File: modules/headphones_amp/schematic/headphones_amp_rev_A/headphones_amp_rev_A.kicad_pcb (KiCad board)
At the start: 2 copper layers, 120 x 100 mm, 127 parts, among them J1 AudioJack3_SwitchTR, J2 AudioJack3_SwitchTR, J3 Conn_01x02, J4 Conn_01x02, J5 Conn_01x02, J6 Conn_01x02, J7 Conn_01x02, Q1 BC140, Q10 BC548, Q11 BC548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

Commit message: input stage: improved biasing (more stable version), added component values (validated on prototype) PCB cleanup (useless footprints)
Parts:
- removed C16, C18: 220µ, Capacitor_THT:CP_Radial_D10.0mm_P5.00mm
- removed the D1 at (269.6, 64.6)
- removed the D2 at (324.6, 161.2)
- removed D3: 1N4148, Diode_THT:D_DO-35_SOD27_P7.62mm_Horizontal
- removed the R18 at (110.2, 67.7)
- removed the R23 at (81.8, 108.2)
- removed the R24 at (31.0, 76.0)
- removed the R36 at (48.9, 34.9)
- removed the R4 at (237.8, 50.9)
- removed the R45 at (31.0, 80.0)
- removed R47, R49: 470, Resistor_THT:R_Axial_DIN0207_L6.3mm_D2.5mm_P10.16mm_Horizontal
- removed the SW1 at (141.0, 27.2)
- C10, C3, C9: value 220µ -> 33µF
- C15, C17: value 47µF -> 33µF
- R22, R50: value 470 -> 5.6k
- R23, R48: value 470 -> 4.7k
- R24, R4, R45, R46: value 470 -> 100k
- R36, R51: value 470 -> 2.7k
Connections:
- R24 pad 1: +12V -> Net-(Q18-C)
- R4 pad 1: +12V -> Net-(Q17-C)
- RV3 pad 4: GND -> Net-(J4-Pin_2)
- RV3 pad 6: Net-(J4-Pin_2) -> GND

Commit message: updated pcb layout
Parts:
- moved R3 243.8 mm to (14.4, 144.3)
- moved R5 243.8 mm to (14.4, 152.4)
- moved R8 243.8 mm to (14.4, 164.6)
- moved TP3 243.8 mm to (35.6, 124.5)
- moved R23 163.2 mm to (26.7, 79.0)
- moved R24 163.2 mm to (26.7, 83.0)
- moved R36 163.2 mm to (26.7, 87.1)
- moved R4 163.2 mm to (26.7, 74.9)
- moved R45 163.2 mm to (26.7, 91.1)
- moved R46 163.2 mm to (26.7, 95.2)
- moved R48 163.2 mm to (26.7, 103.3)
- moved R50 163.2 mm to (26.7, 111.4)
- moved R51 163.2 mm to (26.7, 115.4)
- moved C15 163.2 mm to (16.8, 78.7)
- moved C17 163.2 mm to (16.8, 101.8)
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
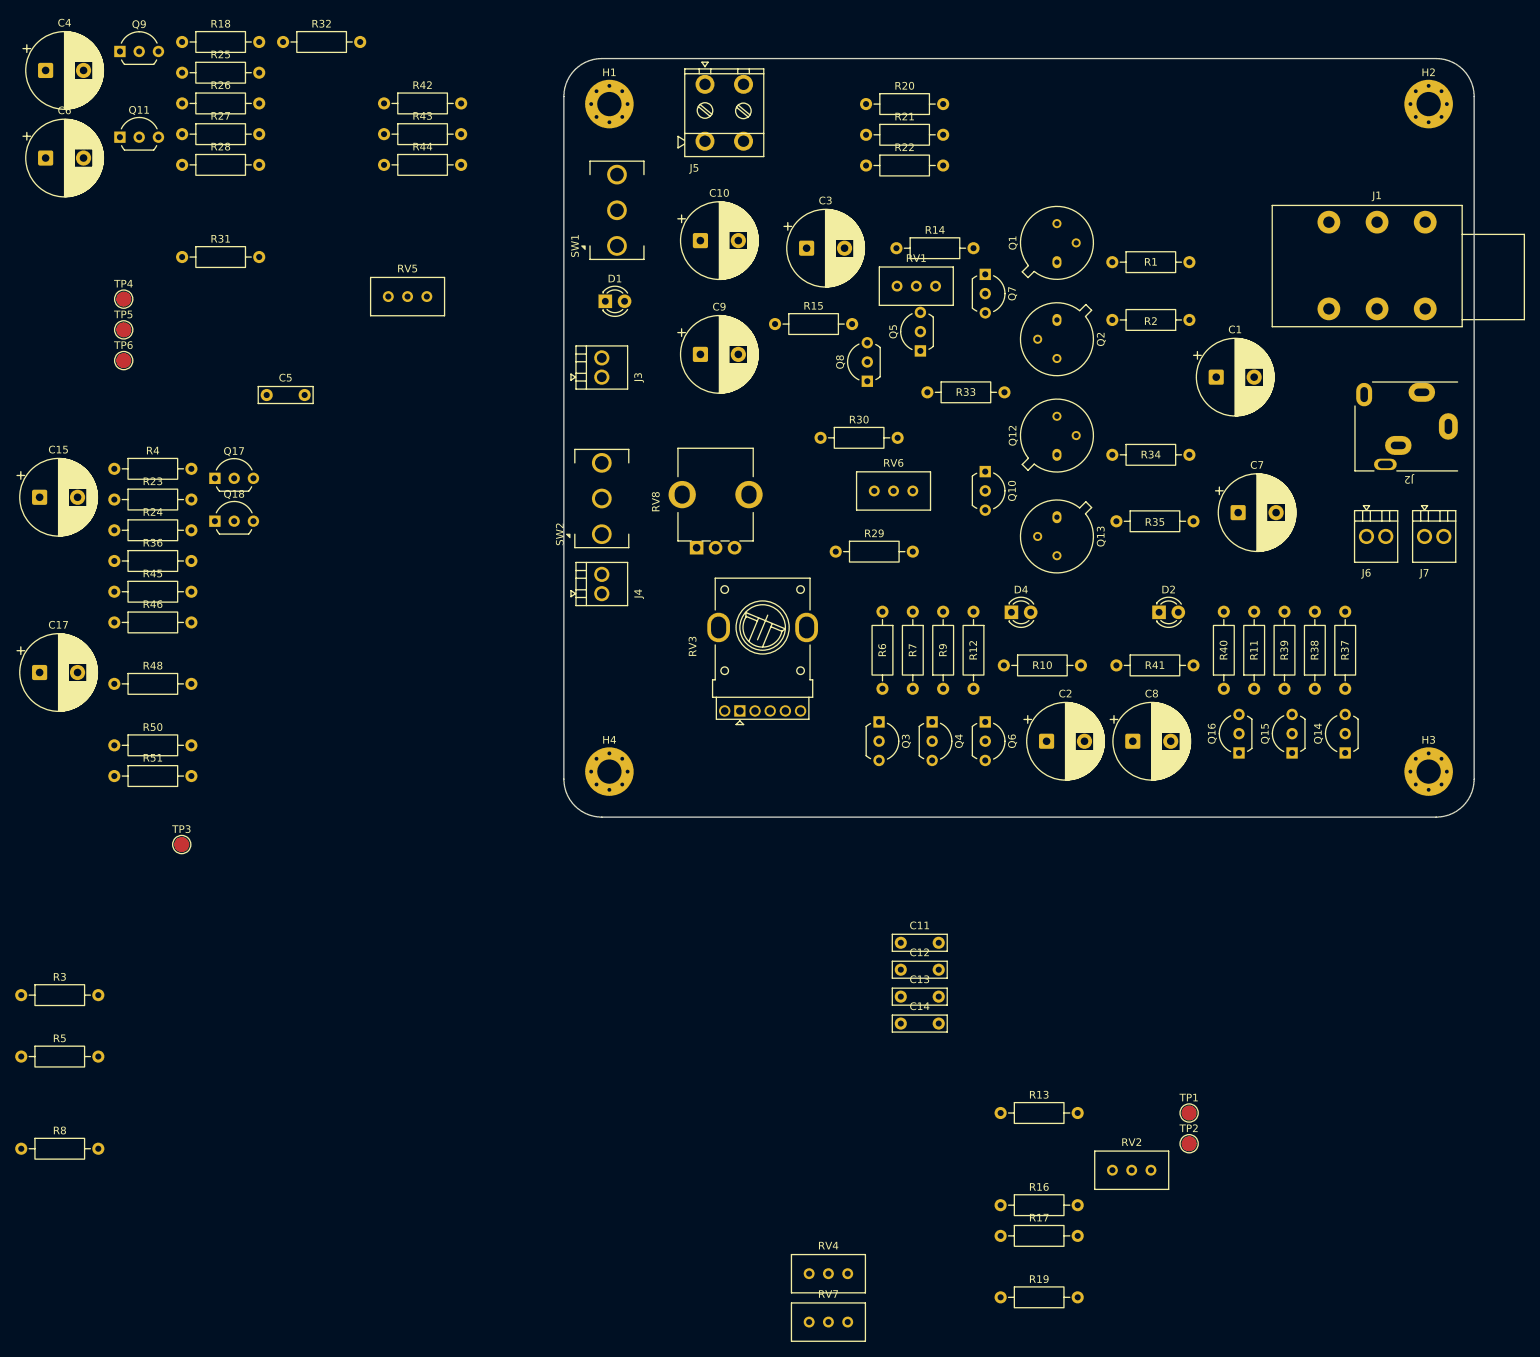
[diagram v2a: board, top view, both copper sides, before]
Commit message: added on board measurements
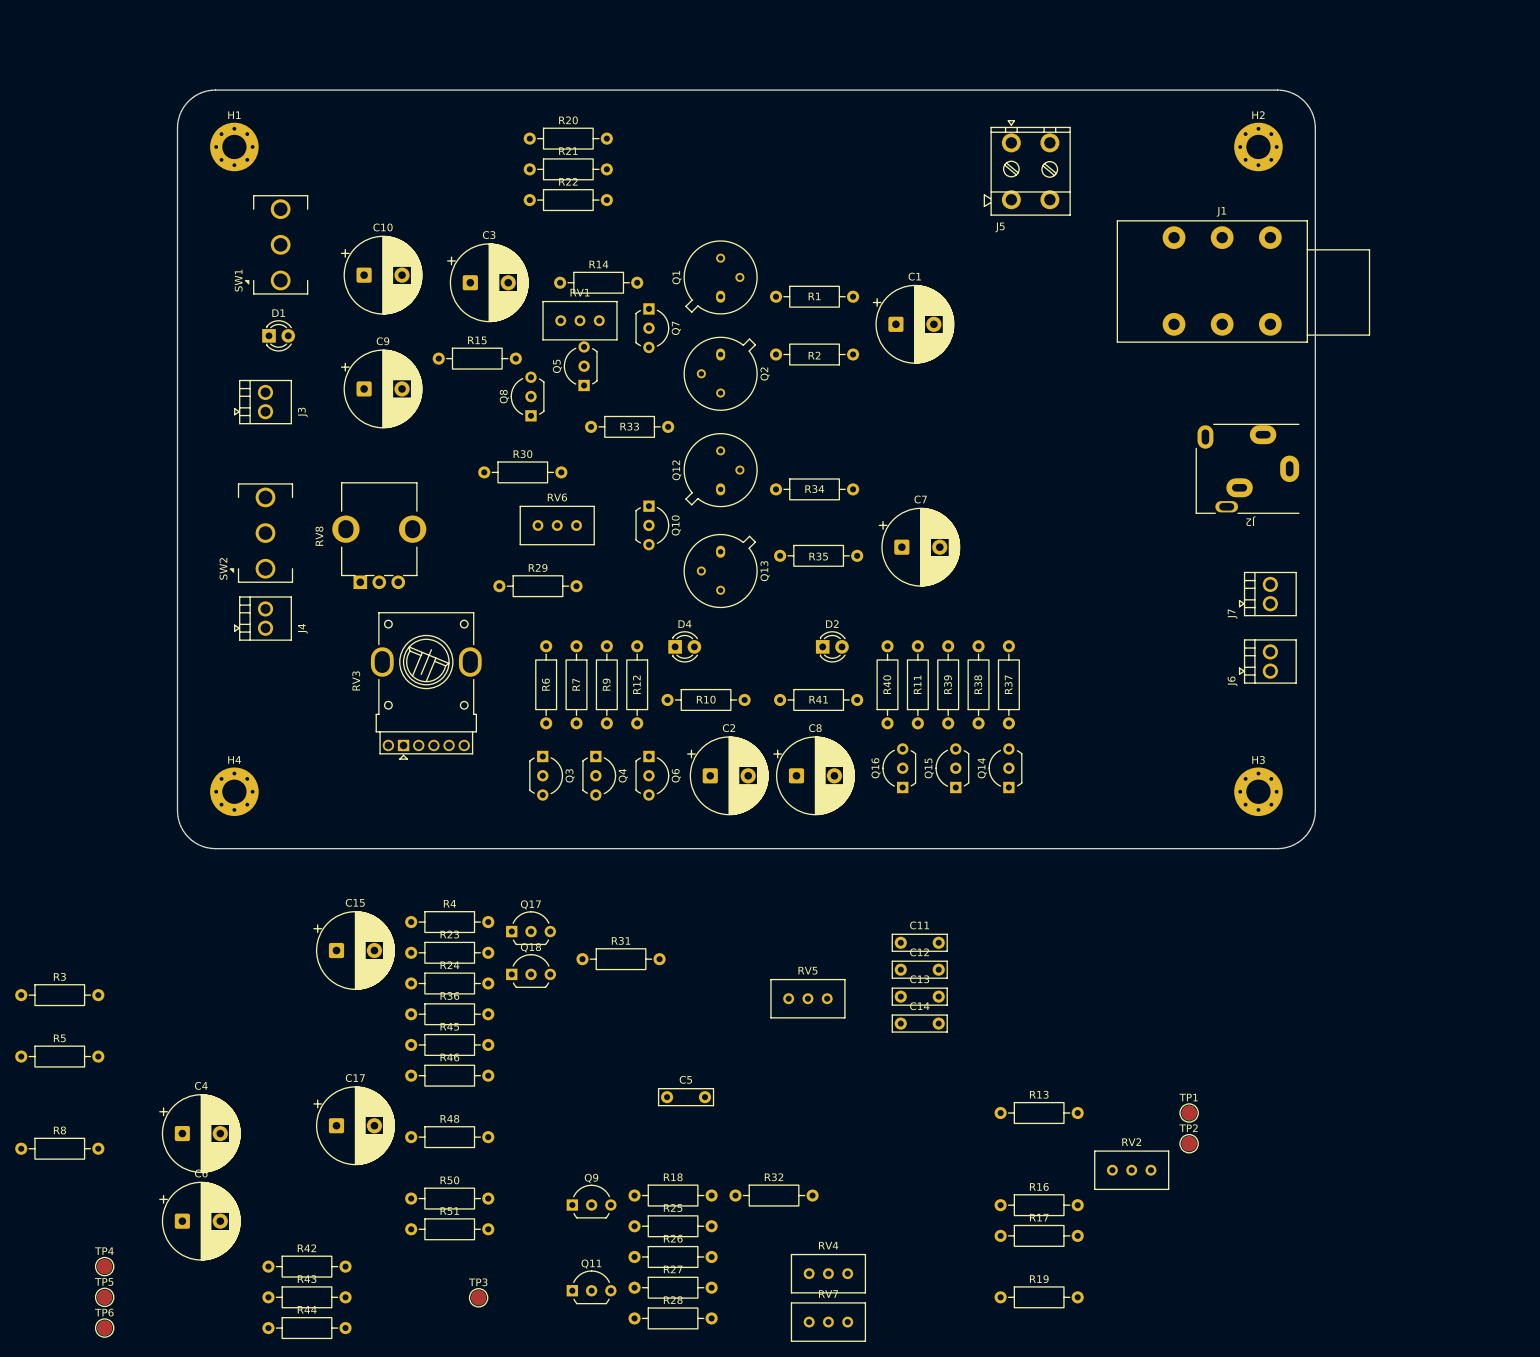
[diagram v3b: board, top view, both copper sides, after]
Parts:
- moved R26 163.3 mm to (95.2, 178.8)
- moved Q11 163.3 mm to (87.0, 183.3)
- moved Q9 163.3 mm to (87.0, 172.0)
- moved R18 163.3 mm to (95.2, 170.7)
- moved R25 163.3 mm to (95.2, 174.8)
- moved R27 163.3 mm to (95.2, 182.9)
- moved R28 163.3 mm to (95.2, 186.9)
- moved R32 163.3 mm to (108.6, 170.7)
- moved R42 154.1 mm to (47.0, 180.1)
- moved R43 154.1 mm to (47.0, 184.2)
- moved R44 154.1 mm to (47.0, 188.2)
- moved C4 141.3 mm to (35.6, 162.6)
- moved C6 141.3 mm to (35.6, 174.1)
- moved TP5 127.6 mm to (25.4, 184.2)
- moved TP4 127.6 mm to (25.4, 180.1)
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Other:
- board size 120 x 100 mm -> 150 x 100 mm

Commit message: progress backup
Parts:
- moved R35 38.5 mm to (152.4, 80.0), turned to 180 degrees
- moved R14 35.3 mm to (120.7, 53.3), turned to 180 degrees
- moved R2 28.5 mm to (152.4, 57.1)
- moved Q13 28.4 mm to (134.6, 81.3)
- moved R34 28.4 mm to (142.2, 76.2)
- moved Q10 28.4 mm to (125.3, 76.2)
- moved R1 28.4 mm to (142.2, 53.3)
- moved Q12 28.2 mm to (134.6, 74.9)
- moved Q7 28.1 mm to (125.3, 53.3)
- moved Q2 28.1 mm to (134.6, 58.4)
- moved Q1 28.0 mm to (134.6, 52.1)
- moved R33 22.0 mm to (110.5, 76.2)
- moved C1 18.3 mm to (145.0, 66.0)
- moved C7 14.8 mm to (144.9, 88.9)
- moved RV1 12.3 mm to (102.9, 55.4), turned to 90 degrees
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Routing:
- net Net-(Q2-E): track 0.00 -> 8.15 mm
- net Net-(Q1-E): track 0.00 -> 8.15 mm

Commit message: PCB progress backup
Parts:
- moved R3 156.5 mm to (124.5, 33.0)
- moved R5 151.7 mm to (115.6, 39.4)
- moved R8 150.2 mm to (120.7, 58.4), turned to 180 degrees
- moved R25 134.1 mm to (50.8, 48.3), turned to -90 degrees
- moved TP1 134.0 mm to (100.3, 44.5)
- moved TP2 133.1 mm to (100.3, 49.5)
- moved TP4 128.1 mm to (100.3, 76.2)
- moved TP5 127.3 mm to (100.3, 81.3)
- moved RV2 124.5 mm to (105.4, 57.1), turned to 90 degrees
- moved TP3 112.0 mm to (92.7, 73.7)
- moved R16 107.4 mm to (110.5, 69.8), turned to 180 degrees
- moved RV4 99.8 mm to (85.1, 88.9)
- moved Q11 99.0 mm to (120.7, 90.2), turned to 90 degrees
- moved Q17 94.2 mm to (72.8, 41.9), turned to 90 degrees
- moved RV7 92.7 mm to (168.9, 106.7), turned to 90 degrees
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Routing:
- net Net-(Q2-E): track 8.15 -> 0.00 mm
- net Net-(Q1-E): track 8.15 -> 0.00 mm

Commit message: PCB progress backup
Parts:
- moved C11 97.5 mm to (142.2, 40.6), turned to 90 degrees
- moved C12 89.6 mm to (142.2, 52.1), turned to -90 degrees
- moved R4 84.1 mm to (59.7, 50.8)
- moved C13 73.1 mm to (142.2, 72.3), turned to 90 degrees
- moved C10 67.2 mm to (81.4, 113.0)
- moved C14 65.3 mm to (142.2, 83.9), turned to -90 degrees
- moved Q18 60.1 mm to (73.7, 81.7)
- moved R22 28.0 mm to (59.7, 57.1)
- moved C9 25.3 mm to (56.0, 39.4)
- moved C1 20.0 mm to (161.3, 68.5), turned to 90 degrees
- moved C7 18.1 mm to (161.3, 81.3), turned to 90 degrees
- moved RV4 16.2 mm to (96.5, 100.3), turned to 90 degrees
- moved R41 13.6 mm to (142.2, 97.8), turned to -90 degrees
- moved R10 7.65 mm to (114.3, 97.8), turned to -90 degrees
- moved D4 7.34 mm to (121.9, 102.9)
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
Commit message: PCB progress backup All parts finally fit in the board!
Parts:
- C6: value 220µ -> 33µF
- moved R19 160.2 mm to (94.0, 31.8)
- moved R43 158.7 mm to (148.6, 62.2), turned to -90 degrees
- moved R17 149.0 mm to (94.0, 35.6)
- moved C4 129.5 mm to (53.4, 34.3)
- moved R44 128.3 mm to (86.4, 66.0), turned to -90 degrees
- moved TP6 125.6 mm to (95.2, 83.8)
- moved C5 124.7 mm to (53.4, 41.9)
- moved C6 120.0 mm to (92.8, 68.6)
- moved R28 101.7 mm to (110.5, 86.4)
- moved R13 100.3 mm to (148.6, 59.7), turned to 90 degrees
- moved R50 97.9 mm to (57.1, 73.7)
- moved R51 97.7 mm to (67.3, 77.5), turned to 180 degrees
- moved R48 97.4 mm to (57.1, 66.0)
- moved R36 97.3 mm to (67.3, 49.5), turned to 180 degrees
- moved R46 94.8 mm to (53.3, 61.0), turned to 90 degrees
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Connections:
- C6 pad 1: Net-(RV8-B) -> Net-(C6-Pad1)
- SW2 pad 1: unconnected-(SW2-Pad1) -> Net-(Q8-C)
- SW2 pad 2: unconnected-(SW2-Pad2) -> Net-(C6-Pad1)
- SW2 pad 3: unconnected-(SW2-Pad3) -> Net-(RV8-B)
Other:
- board text added: "Balance"
- board text added: "L"
- board text added: "Overload"
- board text added: "R"
- board text added: "Volume"
- board text added: "ヘッドフォンアンプ"
